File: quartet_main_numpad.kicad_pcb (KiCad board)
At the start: 2 copper layers, 18 parts, among them J1 USB_C_Receptacle_USB2.0, J2 AVR-ISP-6, J3 Conn_01x16, J4 Conn_01x04

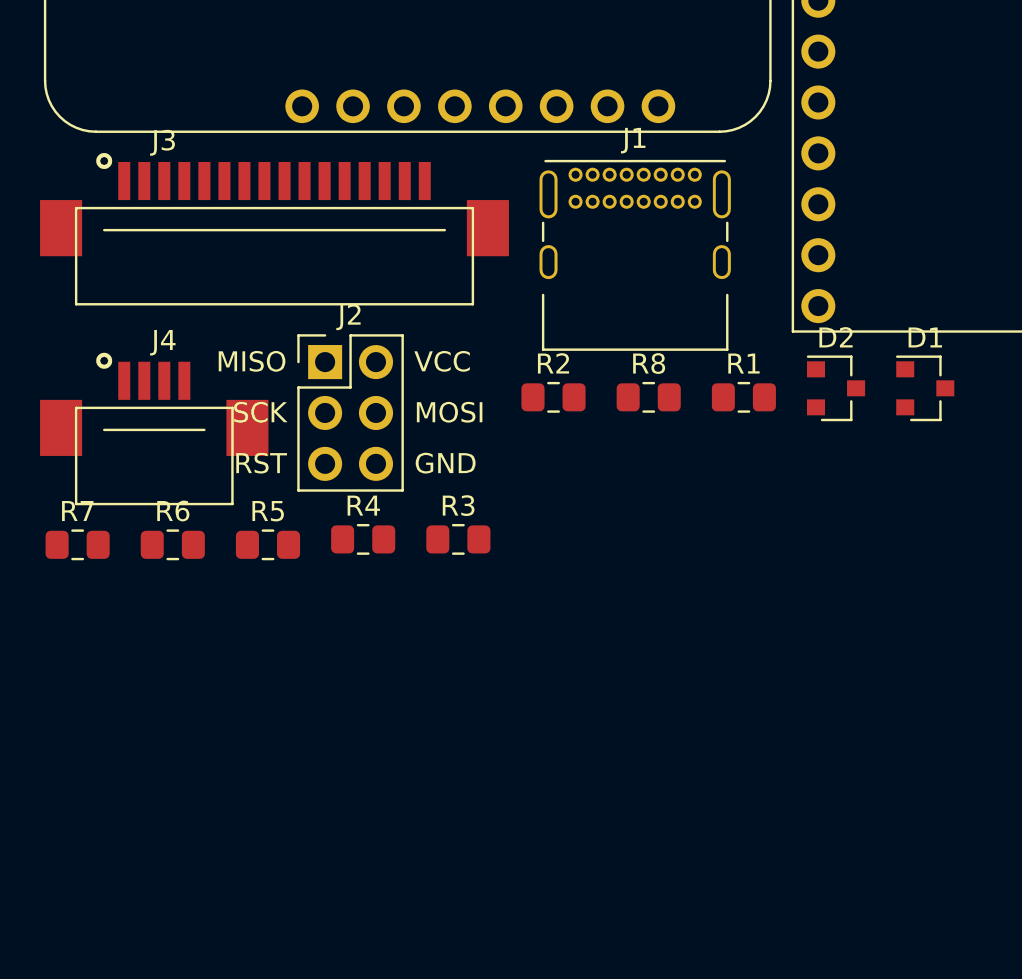
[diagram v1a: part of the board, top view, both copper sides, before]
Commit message: Layout and route numpad matrix
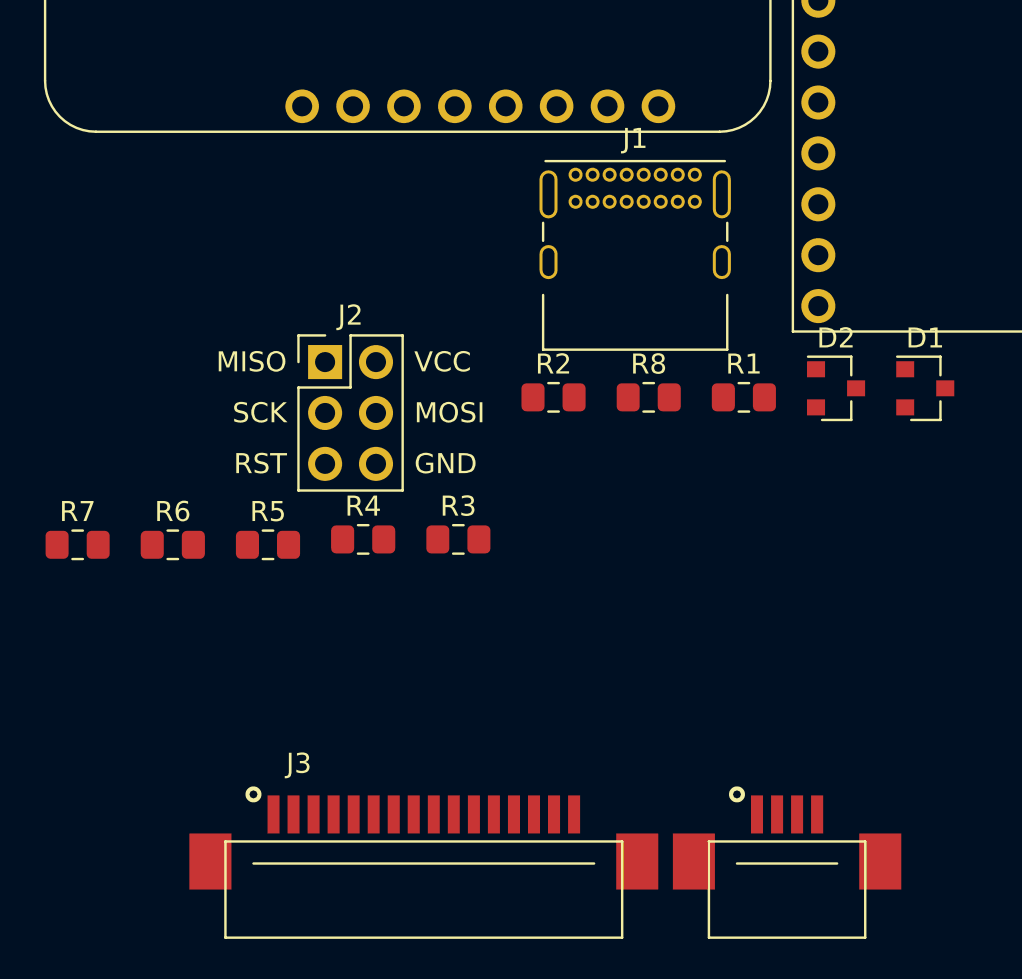
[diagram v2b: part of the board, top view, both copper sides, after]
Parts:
- removed J4: Conn_01x04, Gigahawk:F519-1A7A1-11004-E200
- J3: value Conn_01x16 -> QUARTET_RECV; footprint Gigahawk:F519-1A7A1-11016-E200 -> Gigahawk:QUARTET_RECV_MAIN
- moved J3 32.5 mm to (67.3, 67.3)

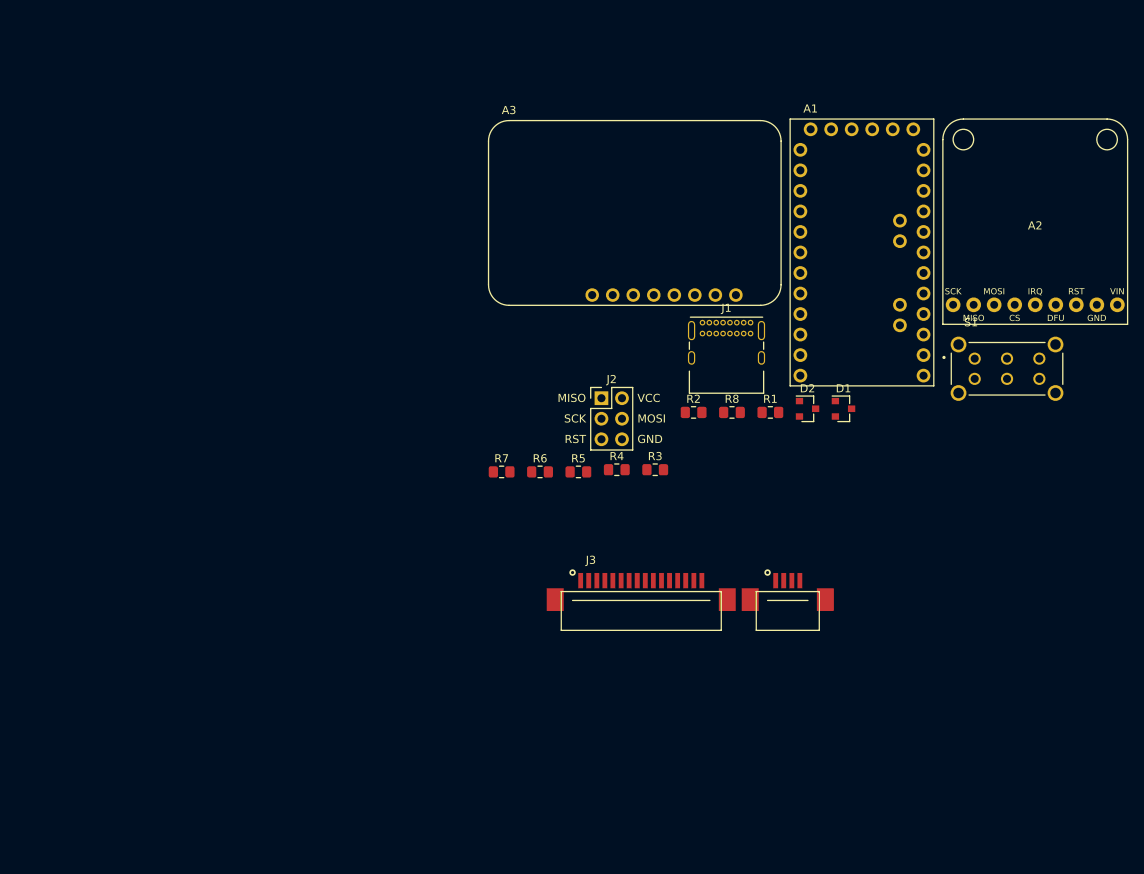
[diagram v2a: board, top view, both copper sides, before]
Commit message: Reroute matrix, redo schematics for feather compat
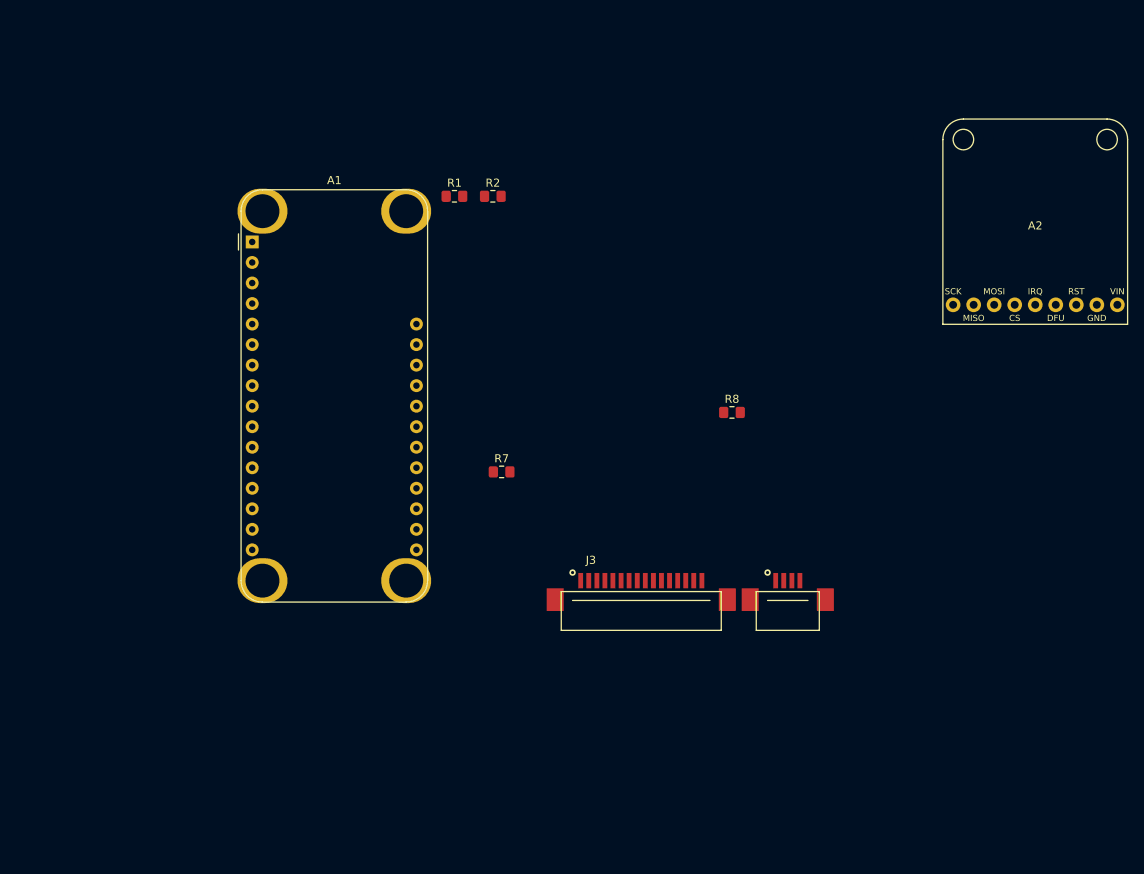
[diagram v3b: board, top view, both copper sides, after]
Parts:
- removed A3: POWERBOOST_1000C, Gigahawk:POWERBOOST_1000C_THT
- removed D1, D2: 3.6V, Diode_SMD:D_SOT-23_ANK
- removed J1: USB_C_Receptacle_USB2.0, Gigahawk:USB_C_Receptacle_GCT_USB4085
- removed J2: AVR-ISP-6, Gigahawk:AVR-ISP-6
- removed R3: 1.5k, Resistor_SMD:R_0805_2012Metric_Pad1.15x1.40mm_HandSolder
- removed R4: DNI, Resistor_SMD:R_0805_2012Metric_Pad1.15x1.40mm_HandSolder
- removed R5, R6: 22R, Resistor_SMD:R_0805_2012Metric_Pad1.15x1.40mm_HandSolder
- removed S1: EG2219, Gigahawk:SW_EG2219
- A1: value ARDUINO_PRO_MINI -> Adafruit_Feather_Generic; footprint Gigahawk:ARDUINO_PRO_MINI_THT -> Gigahawk:Adafruit_Feather_LowProfileSocket
- R1, R2: value 5.1k -> 100k
- moved A1 68.8 mm to (26.7, 25.4)
- moved R1 47.4 mm to (51.7, 19.8)
- moved R2 36.5 mm to (56.4, 19.8)
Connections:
- A1 pad 1: PD1 -> Net-(A1-Pad1)
- A1 pad 10: PD7 -> Net-(A1-Pad10)
- A1 pad 11: PB0 -> SCK
- A1 pad 12: PB1 -> MOSI
- A1 pad 13: PB2 -> MISO
- A1 pad 14: MOSI -> Net-(A1-Pad14)
- A1 pad 15: MISO -> Net-(A1-Pad15)
- A1 pad 16: SCK -> Net-(A1-Pad16)
- A1 pad 17: BLE_CS -> SDA
- A1 pad 18: BLE_IRQ -> SCL
- A1 pad 19: PC2 -> Net-(A1-Pad19)
- A1 pad 2: PD0 -> +3V3
- A1 pad 20: PC3 -> Net-(A1-Pad20)
- A1 pad 21: +5V -> Net-(A1-Pad21)
- A1 pad 22: RST -> Net-(A1-Pad22)
- A1 pad 23: GND -> Net-(A1-Pad23)
- A1 pad 25: (no net) -> Net-(A1-Pad25)
- A1 pad 26: (no net) -> Net-(A1-Pad26)
- A1 pad 27: (no net) -> Net-(A1-Pad27)
- A1 pad 28: (no net) -> +BATT
- A1 pad 3: RST -> Net-(A1-Pad3)
- A1 pad 5: USB_D+ -> BAT_MEAS
- A1 pad 6: USB_D- -> Net-(A1-Pad6)
- A1 pad 7: BLE_RST -> Net-(A1-Pad7)
- A1 pad 8: PD5 -> Net-(A1-Pad8)
- A1 pad 9: PD6 -> Net-(A1-Pad9)
- R1 pad 1: GND -> +BATT
- R1 pad 2: Net-(J1-PadA5) -> BAT_MEAS
- R2 pad 1: GND -> BAT_MEAS
- R2 pad 2: Net-(J1-PadB5) -> GND
- R7 pad 1: +5V -> +3V3
- R8 pad 1: +5V -> +3V3

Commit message: Finish and route quartet mainboard
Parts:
- added H1: TopLeft(3.81,3.81), MountingHole:MountingHole_2.2mm_M2_Pad, F.Cu at (3.81, 3.81)
- added H2: TopRight(96.19,3.81), MountingHole:MountingHole_2.2mm_M2_Pad, F.Cu at (96.2, 3.81)
- added H3: BottomLeft(3.81,96.19), MountingHole:MountingHole_2.2mm_M2_Pad, F.Cu at (3.81, 96.2)
- added H4: BottomRight(96.19,96.19), MountingHole:MountingHole_2.2mm_M2_Pad, F.Cu at (96.2, 96.2)
- added H5: Center(51,41), MountingHole:MountingHole_2.2mm_M2_Pad, F.Cu at (51.0, 41.0)
- added H6: ConnectorPos(85.09,39.37), Gigahawk:DOT, F.Cu at (85.1, 39.4)
- added S1: EG2219, Gigahawk:SW_EG2219, F.Cu at (59.7, 6.60)
- added SW1: SW_SPDT, Button_Switch_THT:SW_E-Switch_EG1224_SPDT_Angled, F.Cu at (59.7, 6.60)
- added SW2: SW_Push, Button_Switch_SMD:SW_SPST_TL3342, F.Cu at (14.2, 10.9)
- added TP1: TestPoint, TestPoint:TestPoint_Pad_1.0x1.0mm, F.Cu at (47.8, 17.3)
- added TP2: TestPoint, TestPoint:TestPoint_Pad_1.0x1.0mm, F.Cu at (35.8, 83.3)
- added TP3: TestPoint, TestPoint:TestPoint_Pad_1.0x1.0mm, F.Cu at (88.9, 37.3)
- added TP4: TestPoint, TestPoint:TestPoint_Pad_1.0x1.0mm, F.Cu at (40.9, 83.3)
- moved A2 100.8 mm to (33.3, 80.5)
- moved R8 33.4 mm to (52.7, 48.0), turned to 90 degrees
- moved J3 33.1 mm to (85.1, 39.4), turned to 270 degrees
- moved R2 28.2 mm to (28.4, 16.0), turned to 90 degrees
- moved R1 19.1 mm to (32.8, 17.0)
- moved A1 18.5 mm to (23.6, 7.11)
- moved R7 13.0 mm to (56.5, 40.9), turned to 270 degrees
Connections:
- net Net-(A1-Pad14) renamed RX_MCU
- net Net-(A1-Pad15) renamed TX_MCU
- A1 pad 1: Net-(A1-Pad1) -> ~RESET
- A1 pad 10: Net-(A1-Pad10) -> A5
- A1 pad 16: Net-(A1-Pad16) -> SPARE
- A1 pad 19: Net-(A1-Pad19) -> D0
- A1 pad 20: Net-(A1-Pad20) -> D1
- A1 pad 21: Net-(A1-Pad21) -> D2
- A1 pad 22: Net-(A1-Pad22) -> D3
- A1 pad 23: Net-(A1-Pad23) -> BLE_RST
- A1 pad 24: Net-(A1-Pad24) -> BLE_IRQ
- A1 pad 25: Net-(A1-Pad25) -> BLE_CS
- A1 pad 27: Net-(A1-Pad27) -> EN
- A1 pad 5: BAT_MEAS -> A0
- A1 pad 6: Net-(A1-Pad6) -> A1
- A1 pad 7: Net-(A1-Pad7) -> A2
- A1 pad 8: Net-(A1-Pad8) -> A3
- A1 pad 9: Net-(A1-Pad9) -> A4
- A2 pad 9: +5V -> +3V3
- J3 pad 1: PD0 -> D0
- J3 pad 10: PC3 -> A5
- J3 pad 11: ADC7 -> SPARE
- J3 pad 17: +5V -> +3V3
- J3 pad 18: +5V -> +3V3
- J3 pad 2: PD1 -> D1
- J3 pad 3: PD5 -> D2
- J3 pad 4: PD6 -> D3
- J3 pad 5: PD7 -> A0
- J3 pad 6: PB0 -> A1
- J3 pad 7: PB1 -> A2
- J3 pad 8: PB2 -> A3
- J3 pad 9: PC2 -> A4
- R1 pad 1: +BATT -> A0
- R1 pad 2: BAT_MEAS -> +BATT
- R2 pad 1: BAT_MEAS -> A0
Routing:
- net SCK: track 0.00 -> 115.6 mm
- net MISO: track 0.00 -> 111.9 mm
- net MOSI: track 0.00 -> 108.6 mm, vias 0 -> 1
- net SPARE: track 0.00 -> 77.2 mm, vias 0 -> 2
- net A5: track 0.00 -> 68.2 mm
- net A4: track 0.00 -> 67.5 mm
- net A3: track 0.00 -> 66.9 mm
- net A2: track 0.00 -> 66.3 mm
- net A1: track 0.00 -> 65.7 mm
- net A0: track 0.00 -> 65.2 mm
- net BLE_CS: track 0.00 -> 58.7 mm
- net BLE_IRQ: track 0.00 -> 55.1 mm
- net D0: track 0.00 -> 53.2 mm, vias 0 -> 1
- net D1: track 0.00 -> 52.8 mm, vias 0 -> 1
- net D2: track 0.00 -> 52.2 mm, vias 0 -> 1
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- added copper zone on B.Cu, net +3V3
- added copper zone on F.Cu, net GND
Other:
- board outline added: 100 x 100 mm

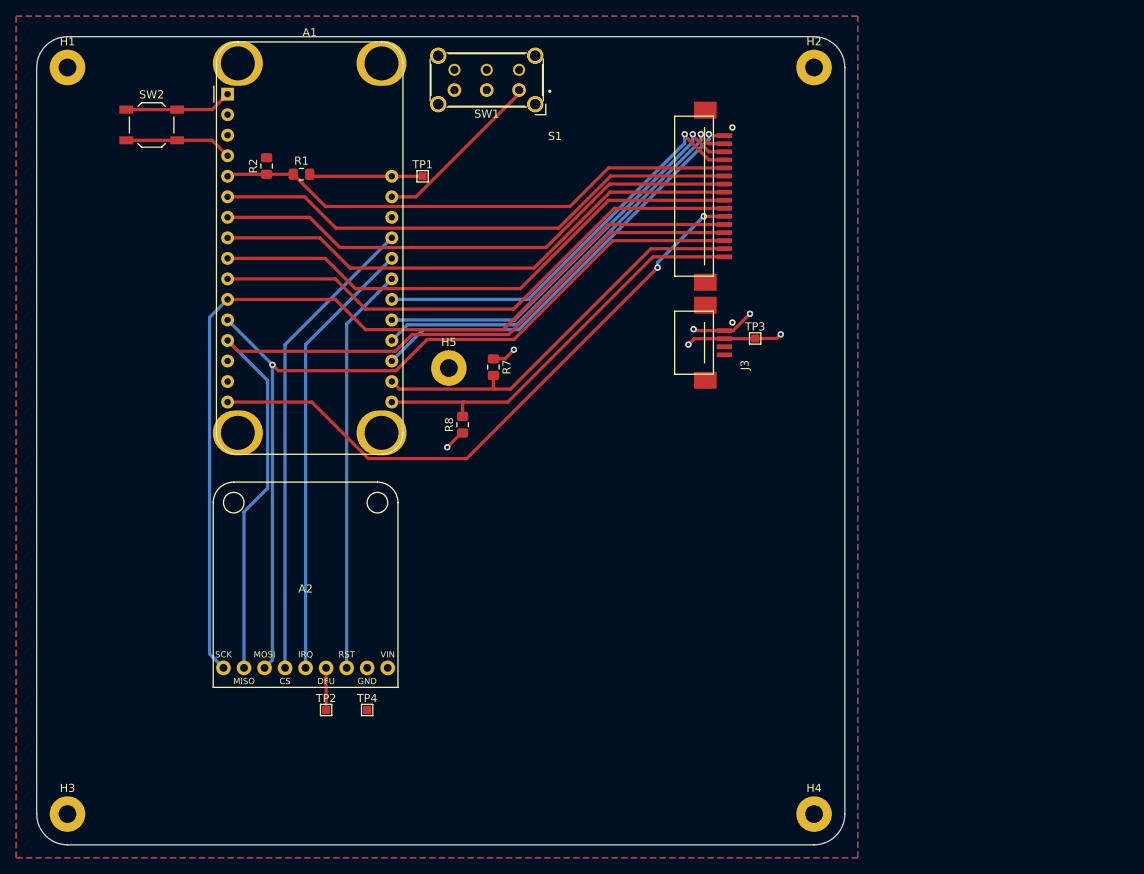
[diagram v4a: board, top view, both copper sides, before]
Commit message: Move bluefruit module on mainboard to accomodate oversize feathers
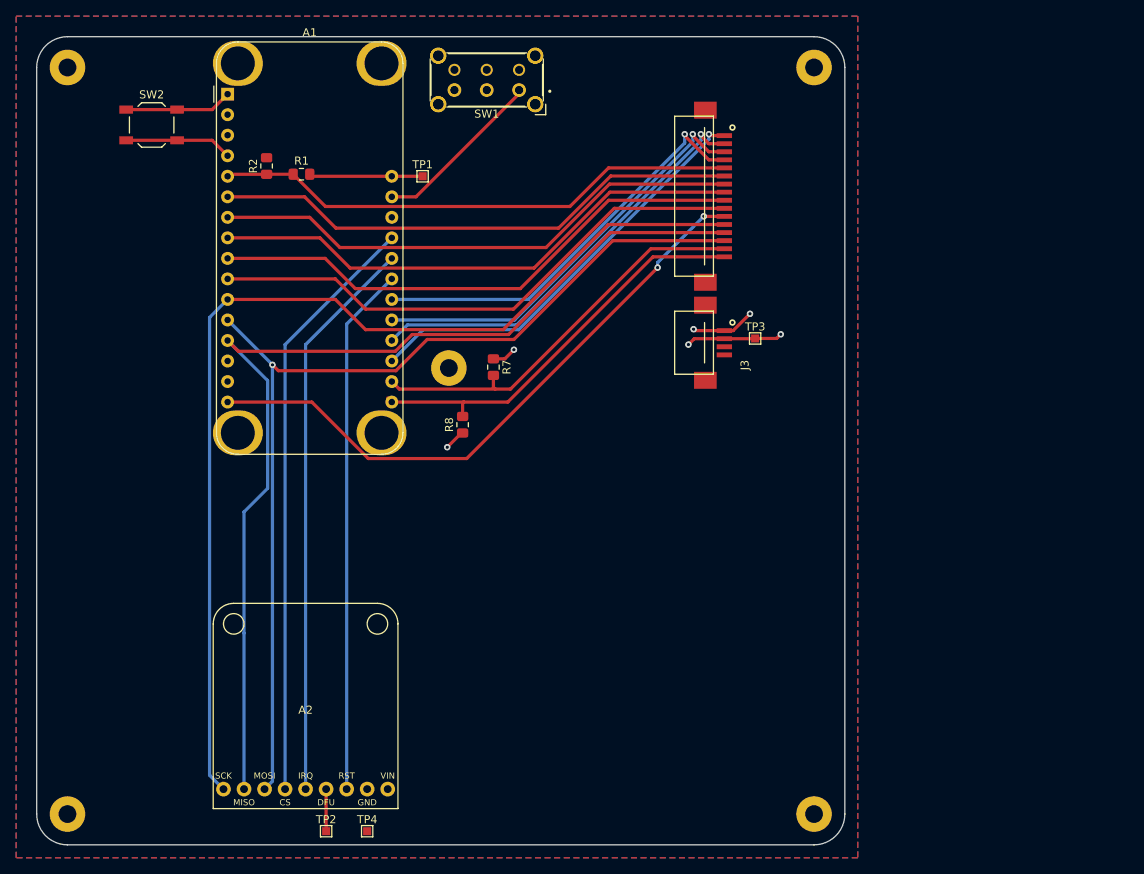
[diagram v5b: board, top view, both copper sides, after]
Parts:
- moved A2 15.0 mm to (33.3, 95.5)
- moved TP2 15.0 mm to (35.8, 98.3)
- moved TP4 15.0 mm to (40.9, 98.3)
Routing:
- net BLE_RST: track 50.4 -> 65.4 mm
- net SCK: track 115.6 -> 130.6 mm
- net MISO: track 111.9 -> 126.9 mm
- net BLE_CS: track 58.7 -> 73.7 mm
- net BLE_IRQ: track 55.1 -> 70.1 mm
- net MOSI: track 108.6 -> 123.6 mm

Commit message: Get ready for JLCPCB
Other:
- board text added: "JLCJLCJLCJLC"
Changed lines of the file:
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@@
   (general
     (thickness 1.6)
-    (drawings 8)
+    (drawings 9)
     (tracks 155)
     (zones 0)
@@
   )
   (setup
-    (last_trace_width 0.4)
+    (last_trace_width 0.25)
     (user_trace_width 0.4)
     (trace_clearance 0.2)
@@
       (outputformat 1)
       (mirror false)
-      (drillshape 1)
+      (drillshape 0)
       (scaleselection 1)
-      (outputdirectory ""))
+      (outputdirectory "export_main_numpad/"))
   )
   (net 0 "")
@@
     (descr "Common footprint for the Adafruit Feather series of boards, https://learn.adafruit.com/adafruit-feather/feather-specification")
     (tags "Adafruit Feather")
-    (fp_text reference A1 (at 10.16 -7.62) (layer F.SilkS)
+    (fp_text reference A1 (at 1.778 46.228) (layer F.SilkS)
       (effects (font (size 1 1) (thickness 0.15)))
     )
@@
   (module Gigahawk:BLUEFRUIT_SPI_FRIEND (layer F.Cu)
     (at 33.274 95.518)
-    (fp_text reference A2 (at 0 -12.2) (layer F.SilkS)
+    (fp_text reference A2 (at -7.874 -26.938) (layer F.SilkS)
       (effects (font (size 1 1) (thickness 0.15)))
     )
@@
       (net 4 BLE_IRQ))
   )
+  (gr_text JLCJLCJLCJLC (at 81.28 20.32 90) (layer F.SilkS)
+    (effects (font (size 0.8 0.8) (thickness 0.15)))
+  )
   (gr_line (start 3.81 0) (end 96.19 0) (angle 90) (layer Edge.Cuts) (width 0.1))
